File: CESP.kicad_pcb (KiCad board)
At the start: 2 copper layers, 55.9 x 44.7 mm, 9 parts

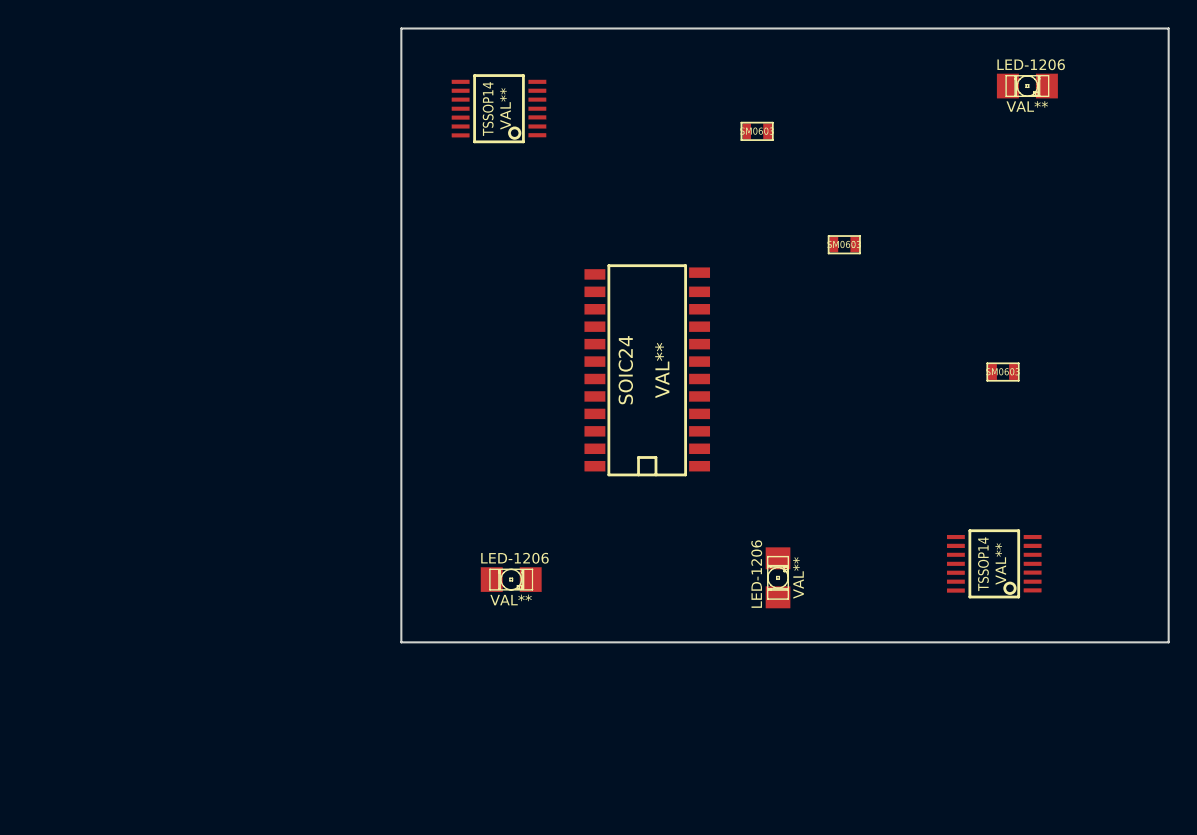
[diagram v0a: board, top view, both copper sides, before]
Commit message: my soldering practice board complete with schematic
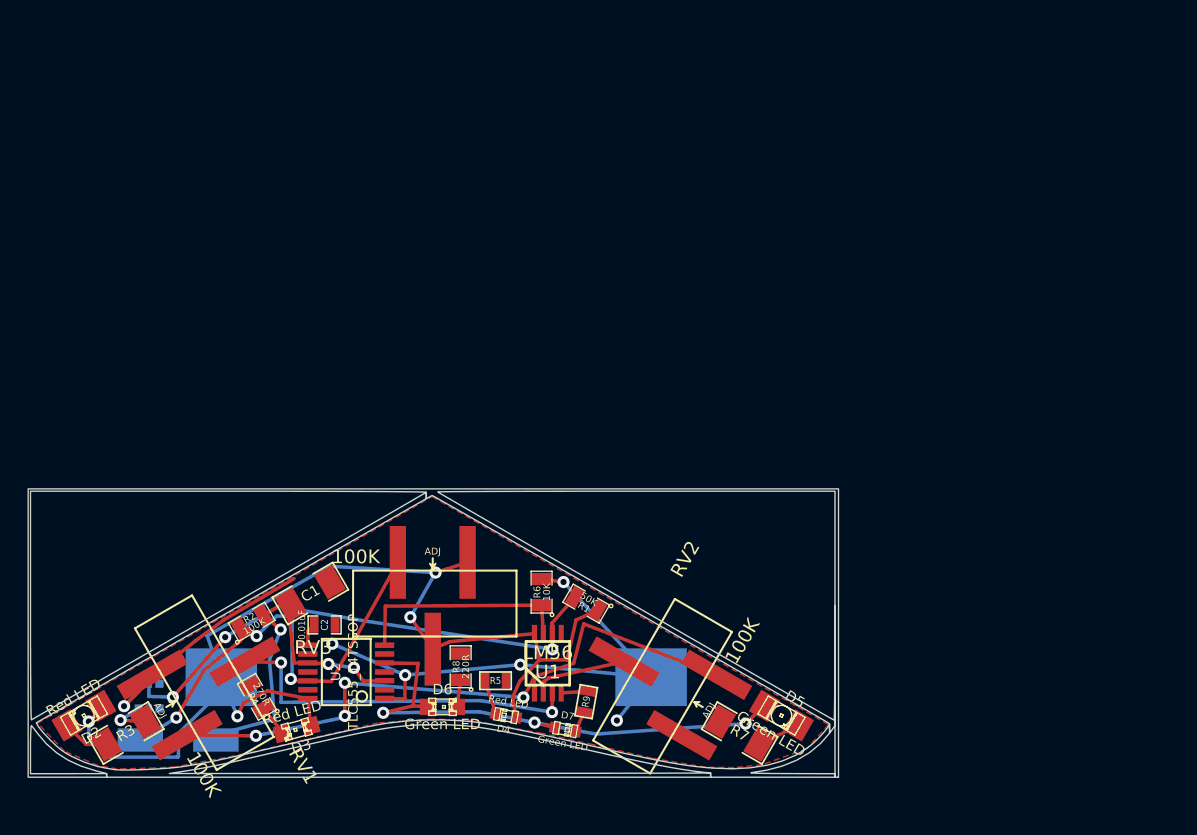
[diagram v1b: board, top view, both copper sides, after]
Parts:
- removed LED-1206 (x3): VAL**, LED-1206
- removed SM0603 (x3): Val**, SM0603
- removed SOIC24: VAL**, SOIC24
- removed TSSOP14 (x2): VAL**, TSSOP14
- added BT1: CR2032, CESP:CR2032_Batt_Holder, B.Cu at (158.5, 143.0)
- added C1: 10uF, SMD_Packages:SM1206, F.Cu at (149.3, 136.9)
- added C2: 0.01uF, SMD_Packages:SM0603_Capa, F.Cu at (150.4, 139.2)
- added D1: FDLL4148, Diodes_SMD:Diode-MiniMELF_Handsoldering, B.Cu at (139.7, 147.6)
- added D2: Red LED, LEDs:LED-1206, F.Cu at (132.8, 145.8)
- added D3: Red LED, LEDs:LED-0805, F.Cu at (148.3, 146.8)
- added D4: Red LED, LEDs:LED-0603, F.Cu at (163.6, 145.8)
- added D5: Green LED, LEDs:LED-1206, F.Cu at (183.6, 145.8)
- added D6: Green LED, LEDs:LED-0805, F.Cu at (159.0, 145.2)
- added D7: Green LED, LEDs:LED-0603, F.Cu at (167.9, 146.8)
- added G***: Outline, CESP:outline3, F.Cu at (158.2, 139.7)
- added Q1: PMBT3904YS, CESP:SOT363, B.Cu at (137.6, 144.4)
- added R1: 50K, SMD_Packages:SM0805, F.Cu at (169.4, 137.6)
- added R2: 100K, SMD_Packages:SM0805, F.Cu at (145.1, 139.0)
- added R3: 270R, SMD_Packages:SM1206, F.Cu at (135.9, 147.1)
- added R4: 270R, SMD_Packages:SM0805, F.Cu at (145.4, 144.4)
- added R5: 270R, SMD_Packages:SM0603, F.Cu at (162.8, 143.3)
- added R6: 10K, SMD_Packages:SM0805, F.Cu at (166.2, 136.8)
- added R7: 220R, SMD_Packages:SM1206, F.Cu at (180.6, 147.1)
- added R8: 220R, SMD_Packages:SM0805, F.Cu at (160.3, 142.2)
- added R9: 220R, SMD_Packages:SM0603, F.Cu at (169.4, 144.8)
- added RV1: 100K, CESP:TRIM_SMD_SIDE_ADJ, F.Cu at (140.0, 144.5)
- added RV2: 100K, CESP:TRIM_SMD_SIDE_ADJ, F.Cu at (176.8, 144.5)
- added RV3: 100K, CESP:TRIM_SMD_SIDE_ADJ, F.Cu at (158.2, 135.6)
- added U1: LM56, SMD_Packages:MSOP_8, F.Cu at (166.6, 142.0)
- added U2: TLC555_14TSSOP, SSOP_Packages:SSOP-14, F.Cu at (151.9, 142.6)
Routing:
- net VCC: track 0.00 -> 79.2 mm, vias 0 -> 4
- net GND: track 0.00 -> 61.8 mm, vias 0 -> 6
- net Net-(RV1-Pad1): track 0.00 -> 46.3 mm, vias 0 -> 4
- net Net-(D5-Pad1): track 0.00 -> 38.6 mm, vias 0 -> 3
- net Net-(Q1-Pad2): track 0.00 -> 37.6 mm, vias 0 -> 3
- net Net-(D1-Pad1): track 0.00 -> 34.4 mm, vias 0 -> 3
- net Net-(RV1-Pad2): track 0.00 -> 26.7 mm, vias 0 -> 2
- net Net-(C1-Pad1): track 0.00 -> 26.7 mm, vias 0 -> 3
- net Net-(R6-Pad1): track 0.00 -> 16.3 mm
- net Net-(RV2-Pad2): track 0.00 -> 6.88 mm
- net Net-(D2-Pad2): track 0.00 -> 3.42 mm
- net Net-(Q1-Pad6): track 0.00 -> 3.39 mm, vias 0 -> 1
- net Net-(D5-Pad2): track 0.00 -> 3.17 mm
- net Net-(D4-Pad2): track 0.00 -> 2.53 mm
- net Net-(D3-Pad2): track 0.00 -> 2.31 mm
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- added copper zone on F.Cu, net GND
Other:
- board size 55.9 x 44.7 mm -> 59 x 21 mm
- net class Default: clearance 0.254 -> 0.127
- rule trace_clearance: 0.254 -> 0.127
- board text removed: "NOTE: THIS IS JUST A TEST BOARD REMOVE ALL COMPONENTS AND CREATE YOUR OWN INCLUDE SCHEMATIC HOOKUPS/NETLIST"
